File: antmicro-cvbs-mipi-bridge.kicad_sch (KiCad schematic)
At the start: 106 parts, among them IC1 ADV7280BCPZ-M, IC2 TLV70018, IC4 SN74AUP1G17DCKR, IC5 SN74AUP1G17DCKR, J1 WE_68715014522_ONE-SIDE, J2 61300211121, J7 61300211121, Q1 NX3008NBKS_2, Q2 BSS138APW, Y1 ABM8G-28.63636MHZ-18-D2Y-T

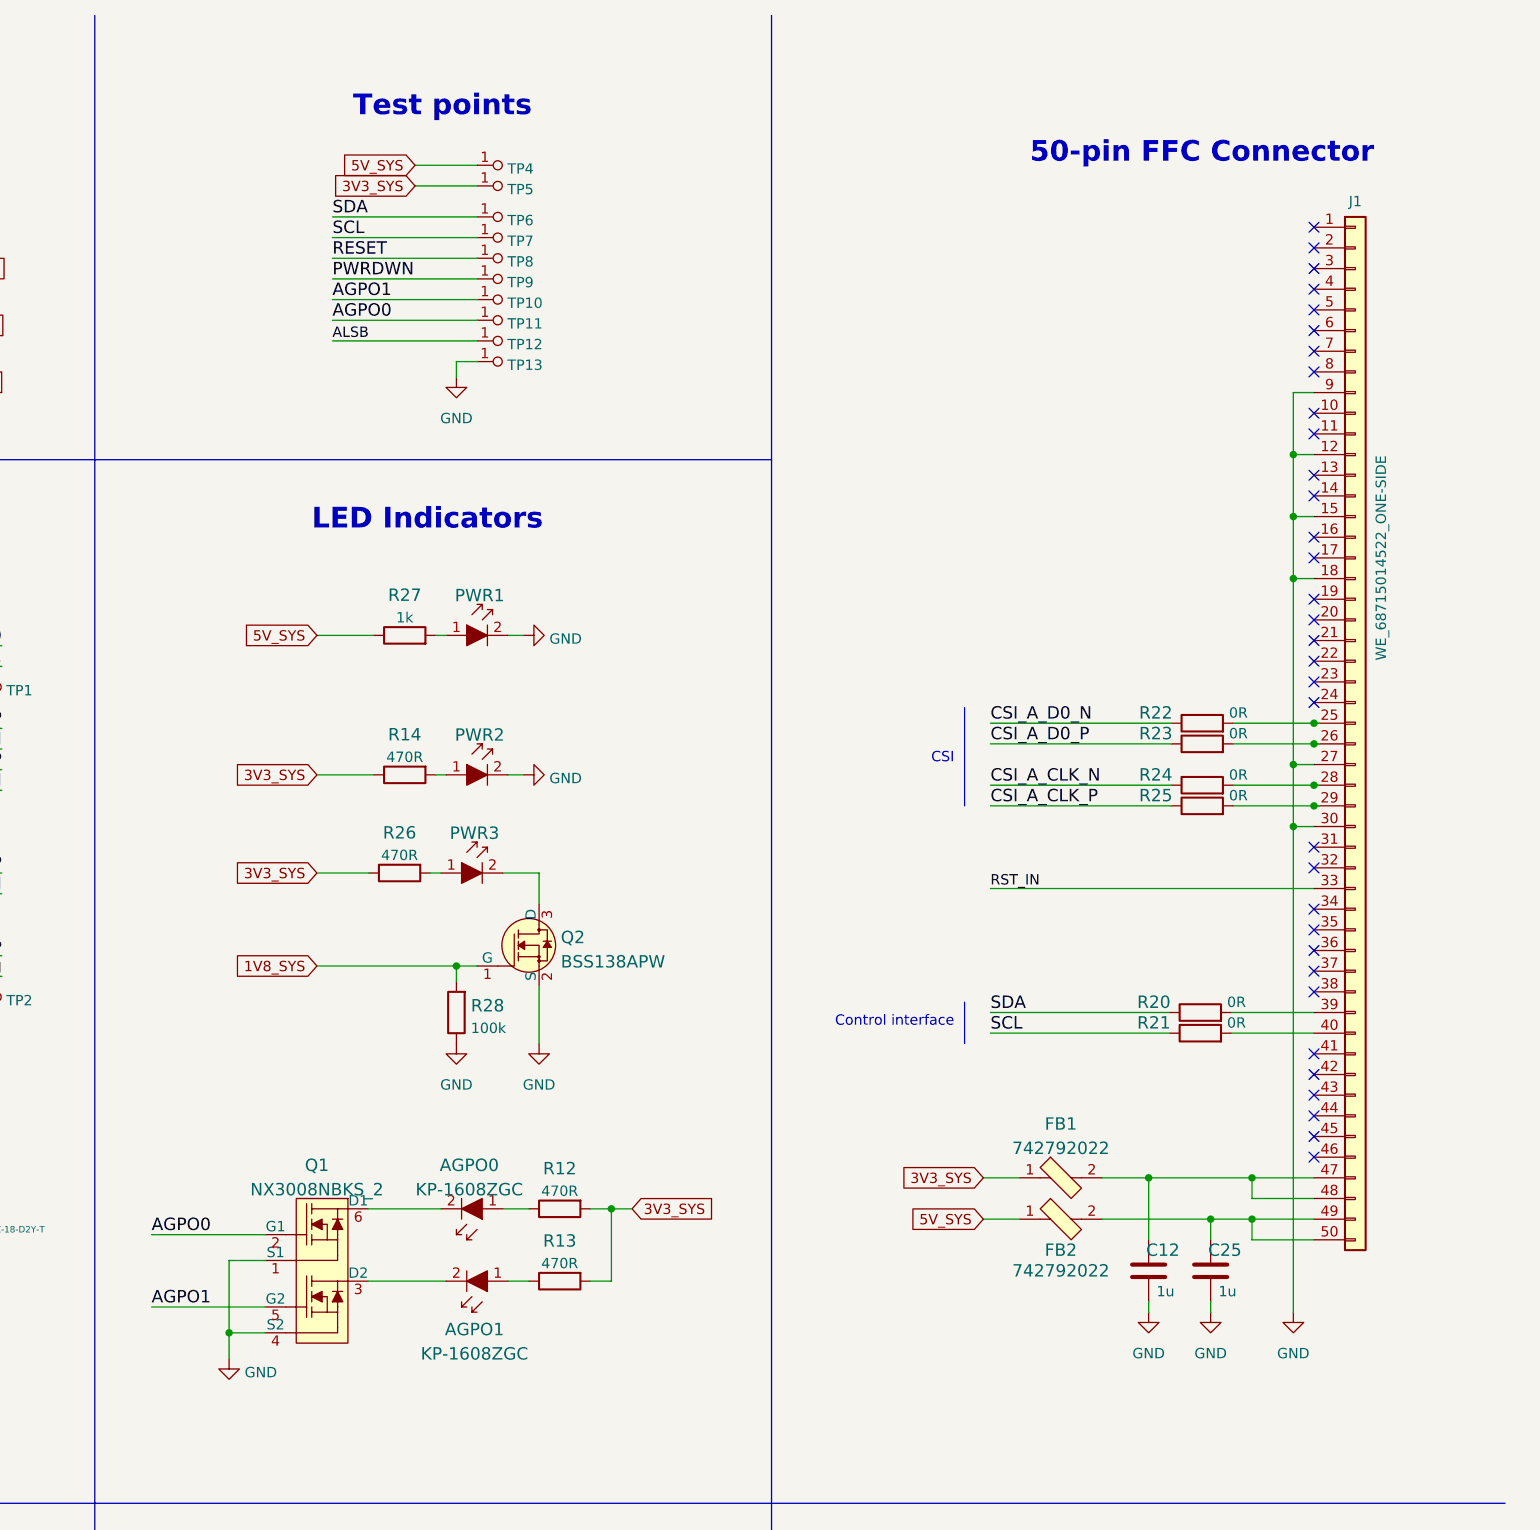
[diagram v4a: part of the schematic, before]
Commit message: Finished placement. Removed 5V net and components. Started routing
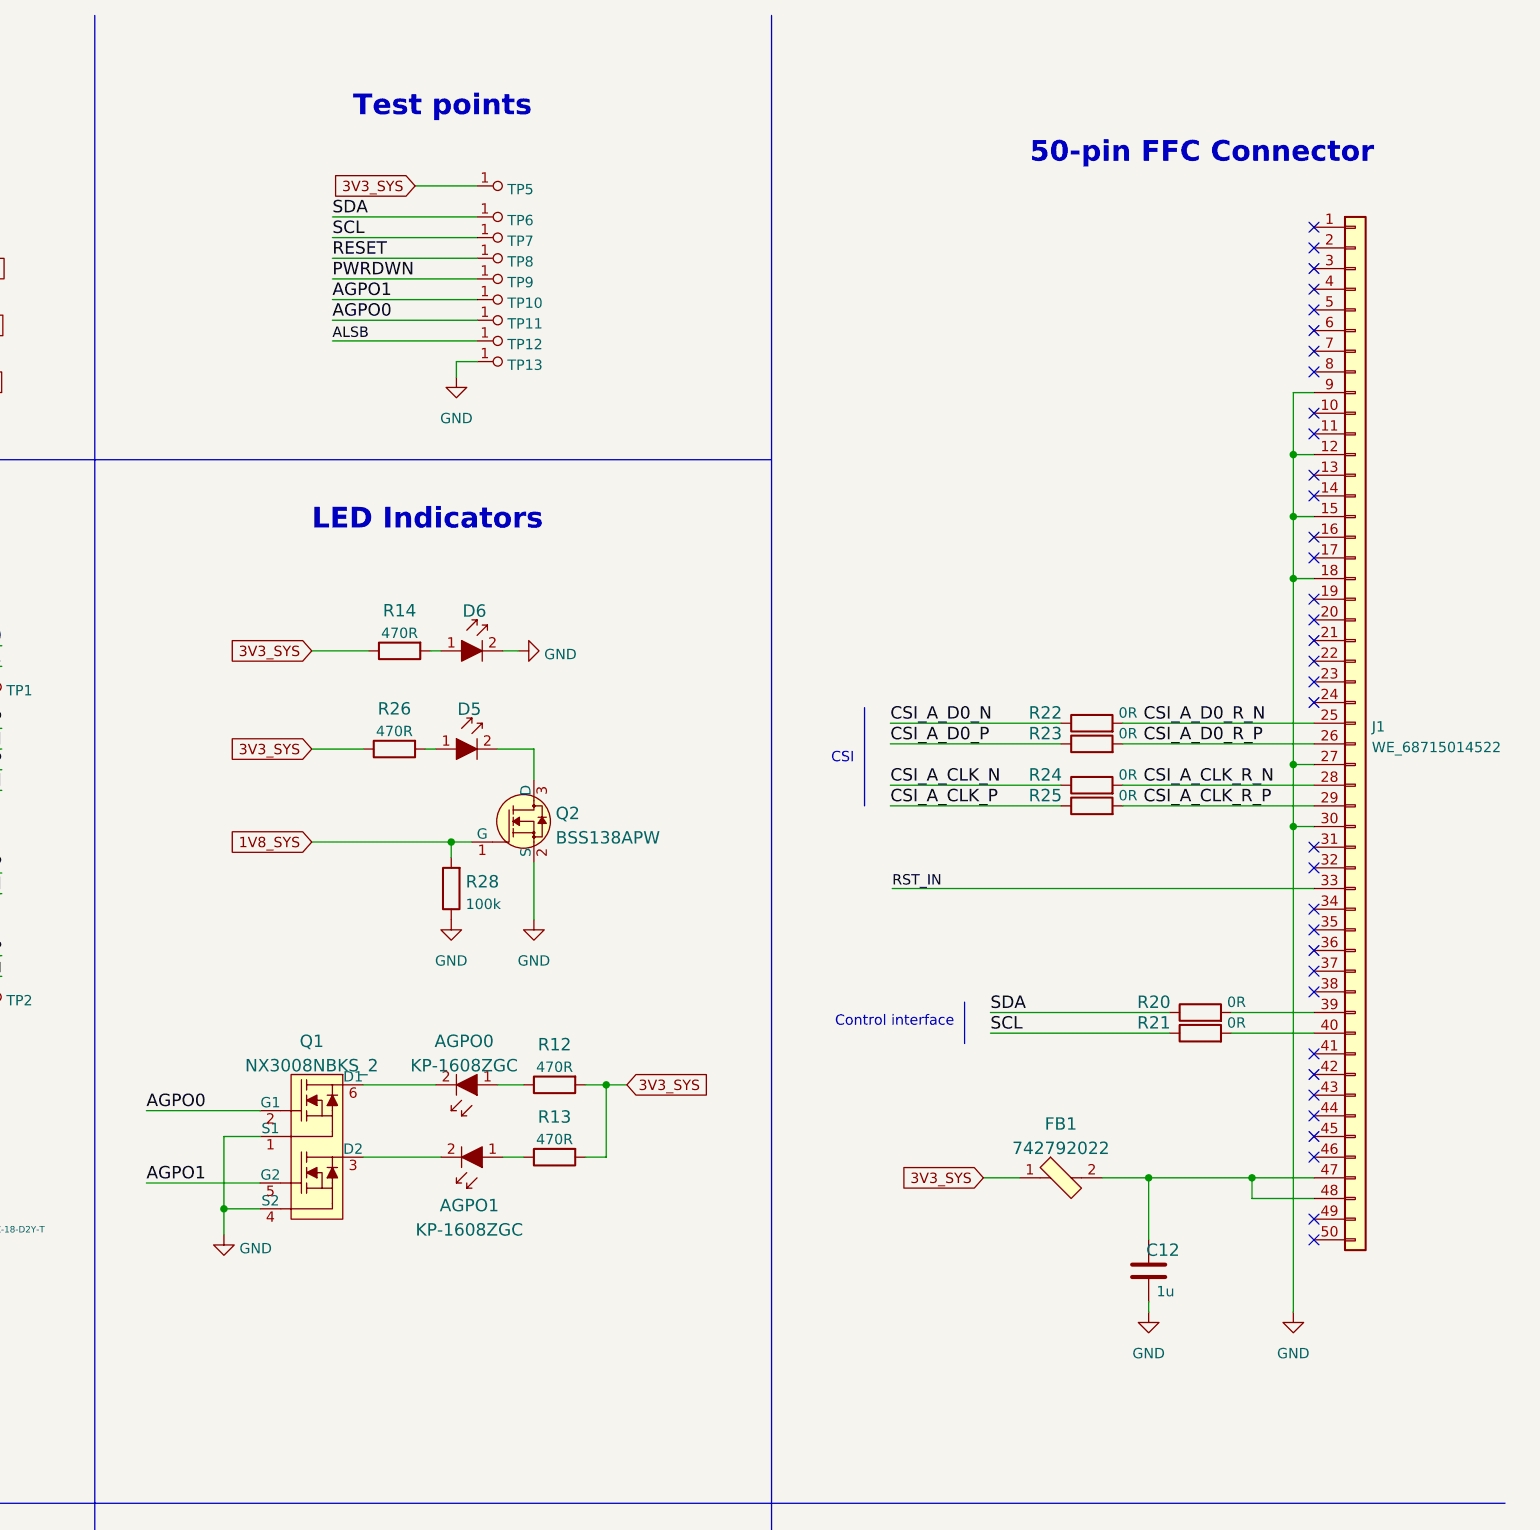
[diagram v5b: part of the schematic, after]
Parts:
- removed C25: C_1u_0603, antmicro-footprints:0603-cap, symbol antmicro-jetson-agx-csi-adapter:C_1u_0603
- removed FB2: 742792022, antmicro-footprints:0805-res, symbol antmicroFerriteBeadsandChips:742792022
- removed J1: WE_68715014522_ONE-SIDE, antmicro-footprints:WE_68715014522_ONE-SIDE, symbol antmicro-jetson-agx-csi-adapter:WE_68715014522_ONE-SIDE
- removed PWR1: KP-1608ZGC, antmicro-footprints:LED_0603, symbol antmicroLEDIndicationDiscrete:KP-1608ZGC
- removed R27: R_1k_0402, antmicro-footprints:0402-res, symbol antmicroResistors0402:R_1k_0402
- removed TP4: TP, antmicro-footprints:TP-R-1.5, symbol antmicroTestPoints:TP
- added J1: WE_68715014522, antmicro-footprints:WE_68715014522, symbol antmicroFCCConnectors:WE_68715014522
- renumbered PWR3 to D5, PWR2 to D6
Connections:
- net GND: now also J1.12 (Pin_12), J1.15 (Pin_15), J1.18 (Pin_18), J1.27 (Pin_27), J1.30 (Pin_30), J1.9 (Pin_9)
- net RST_IN: now also J1.33 (Pin_33)
- net CSI_A_D0_R_N: now reaches R22.2
- net CSI_A_D0_R_N: now also J1.25 (Pin_25)
- net CSI_A_D0_R_P: now reaches R23.2
- net CSI_A_D0_R_P: now also J1.26 (Pin_26)
- net CSI_A_CLK_R_N: now reaches R24.2
- net CSI_A_CLK_R_N: now also J1.28 (Pin_28)
- net CSI_A_CLK_R_P: now reaches R25.2
- net CSI_A_CLK_R_P: now also J1.29 (Pin_29)
- net at R20.2: now also J1.39 (Pin_39)
- net at R21.2: now also J1.40 (Pin_40)
- net at C12.1, FB1.2: now also J1.47 (Pin_47), J1.48 (Pin_48)
- no-connect marks 41 -> 43
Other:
- moved on the sheet: AGPO0, AGPO1, D5, D6, Q1, Q2, R12, R13, R14, R22, R23, R24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

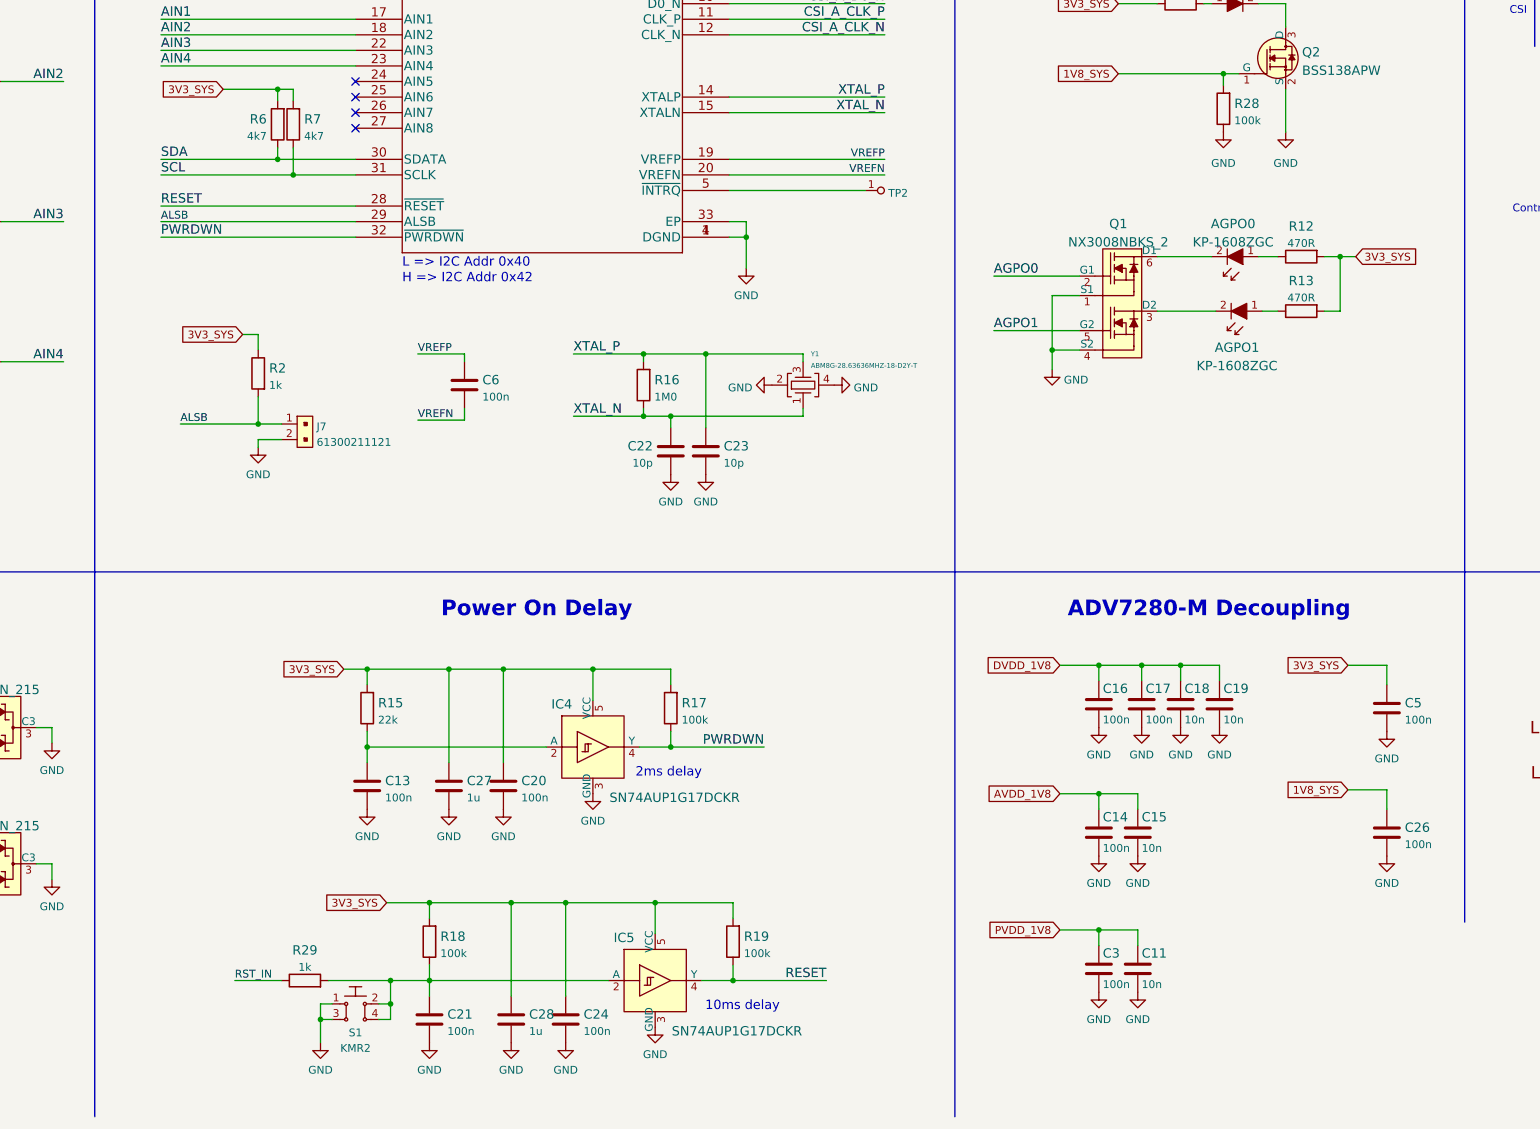
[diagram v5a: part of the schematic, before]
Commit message: Schematic review fixes
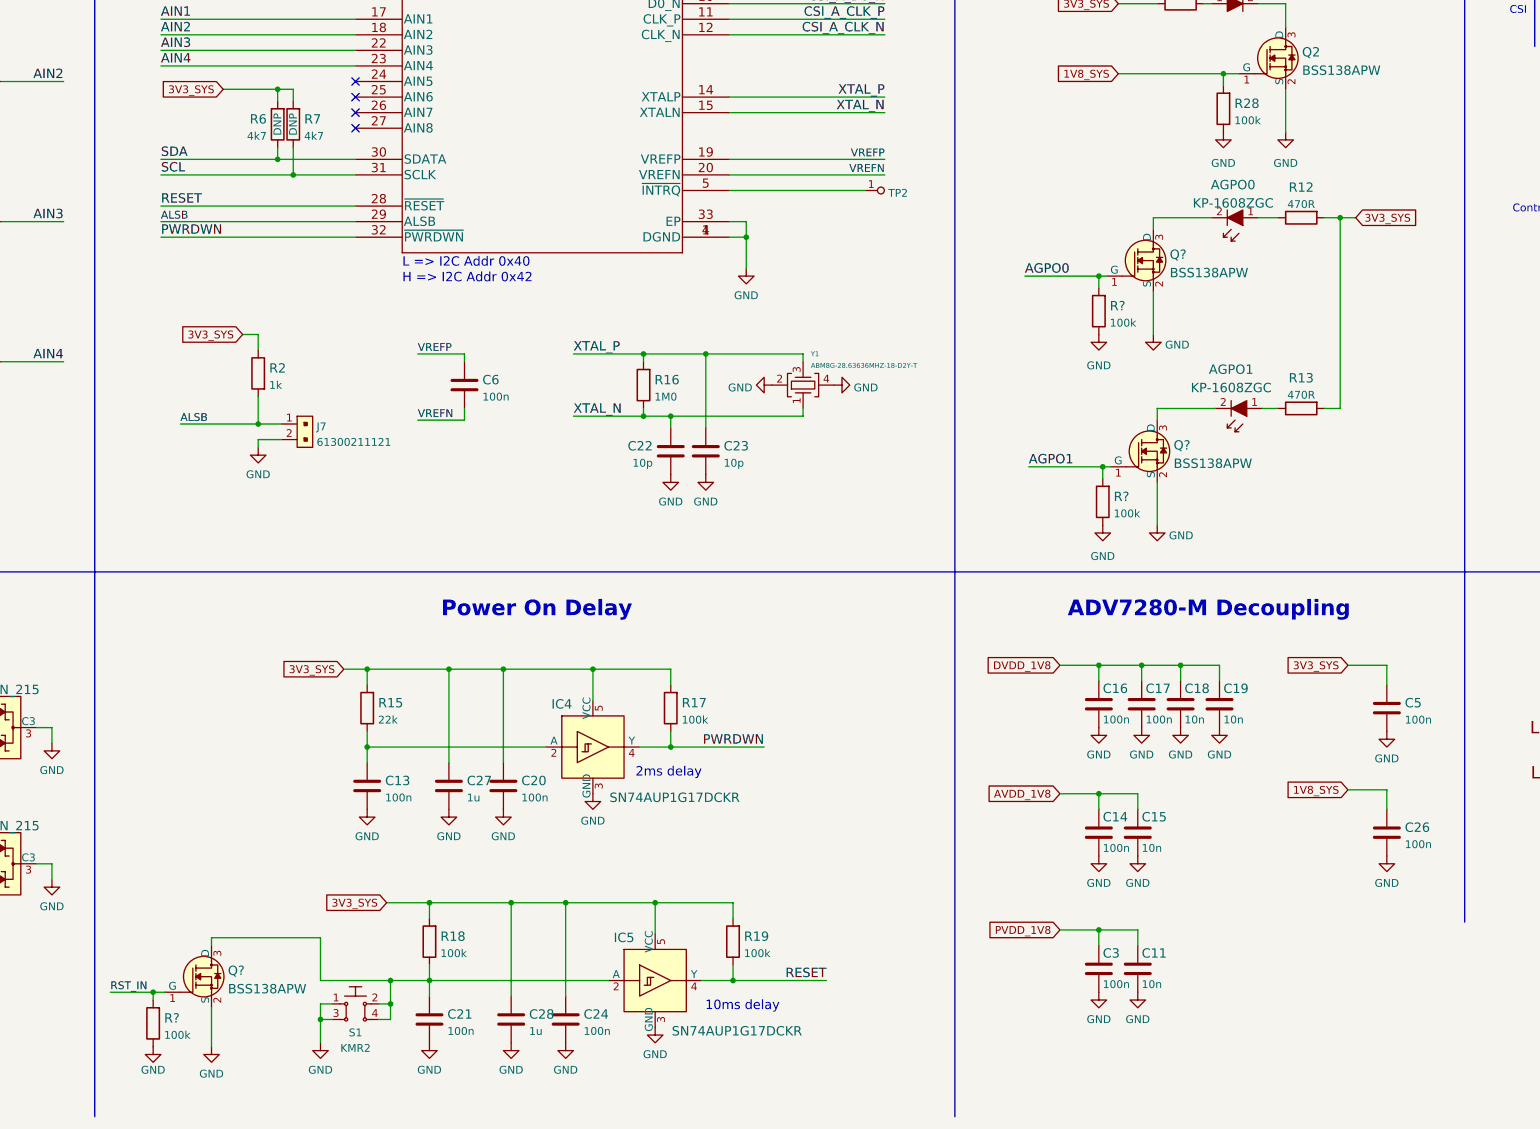
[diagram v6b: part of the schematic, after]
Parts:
- removed Q1: NX3008NBKS_2, antmicro-footprints:SOT-363, symbol antmicroTransistorsFETsMOSFETsArrays:NX3008NBKS_2
- removed R29: R_1k_0402, antmicro-footprints:0402-res, symbol antmicroResistors0402:R_1k_0402
- added Q? (x3): BSS138APW, antmicro-footprints:SC70-3, symbol antmicroTransistorsFETsMOSFETsSingle:BSS138APW
- added R? (x3): R_100k_0402, antmicro-footprints:0402-res, symbol antmicroResistors0402:R_100k_0402
- R6, R7: DNP (none) -> DNP; now left out of the parts list
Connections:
- net AGPO0: now also Q?.1 (G), R?.2
- net AGPO1: now also Q?.1 (G), R?.2
- net GND: now also Q?.2 (S), Q?.2 (S), Q?.2 (S), R?.1, R?.1, R?.1
- net RST_IN: now also Q?.1 (G), R?.2
- net at AGPO0.2: now also Q?.3 (D)
- net at C21.1, IC5.2 (A), R18.1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: now also Q?.3 (D)
- net at AGPO1.2: now also Q?.3 (D)
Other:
- moved on the sheet: AGPO0, AGPO1, R12, R13

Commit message: Fixes adjusted visually. New components annotated
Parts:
- gave numbers to parts that had none: 6
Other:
- moved on the sheet: AGPO0, AGPO1, C21, C24, C28, D5, D6, IC5, Q1, Q2, Q3, Q4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
